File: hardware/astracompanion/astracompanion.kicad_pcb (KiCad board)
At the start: 2 copper layers, 118.5 x 94.8 mm, 124 parts, among them J1 Screw_Terminal_01x02, J10 Conn_01x03_Pin, J2 Screw_Terminal_01x02, J3 Conn_01x03_Pin, J4 USB_C_Receptacle_USB2.0, J5 Conn_01x02_Socket, J6 Micro_SD_Card, J7 Conn_01x04_Socket, J8 testpoint, J9 Encoder_L, Q1 2N3904, Q2 2N3904, Q3 2N7002, Q4 AO3401A, SW1 PTS645, SW2 SW_SPST, SW3 PTS645, SW4 Reset / EN button, SW5 Boot / IO0 button, SW6 PTS645, U1 MT3608_BOOSTER_MODULE, U10 MAX17048G+T10, U11 USBLC6-2SC6, U12 74AHCT125, U13 USBLC6-4SC6, U2 ESP32-S3-DEVKITC-1-N8R8, U3 DRV8833PWP, U4 MAX98357A, U5 MPU-6050, U6 DS3231M, U7 AP2112K-3.3, U8 VL53L0CXV0DH1

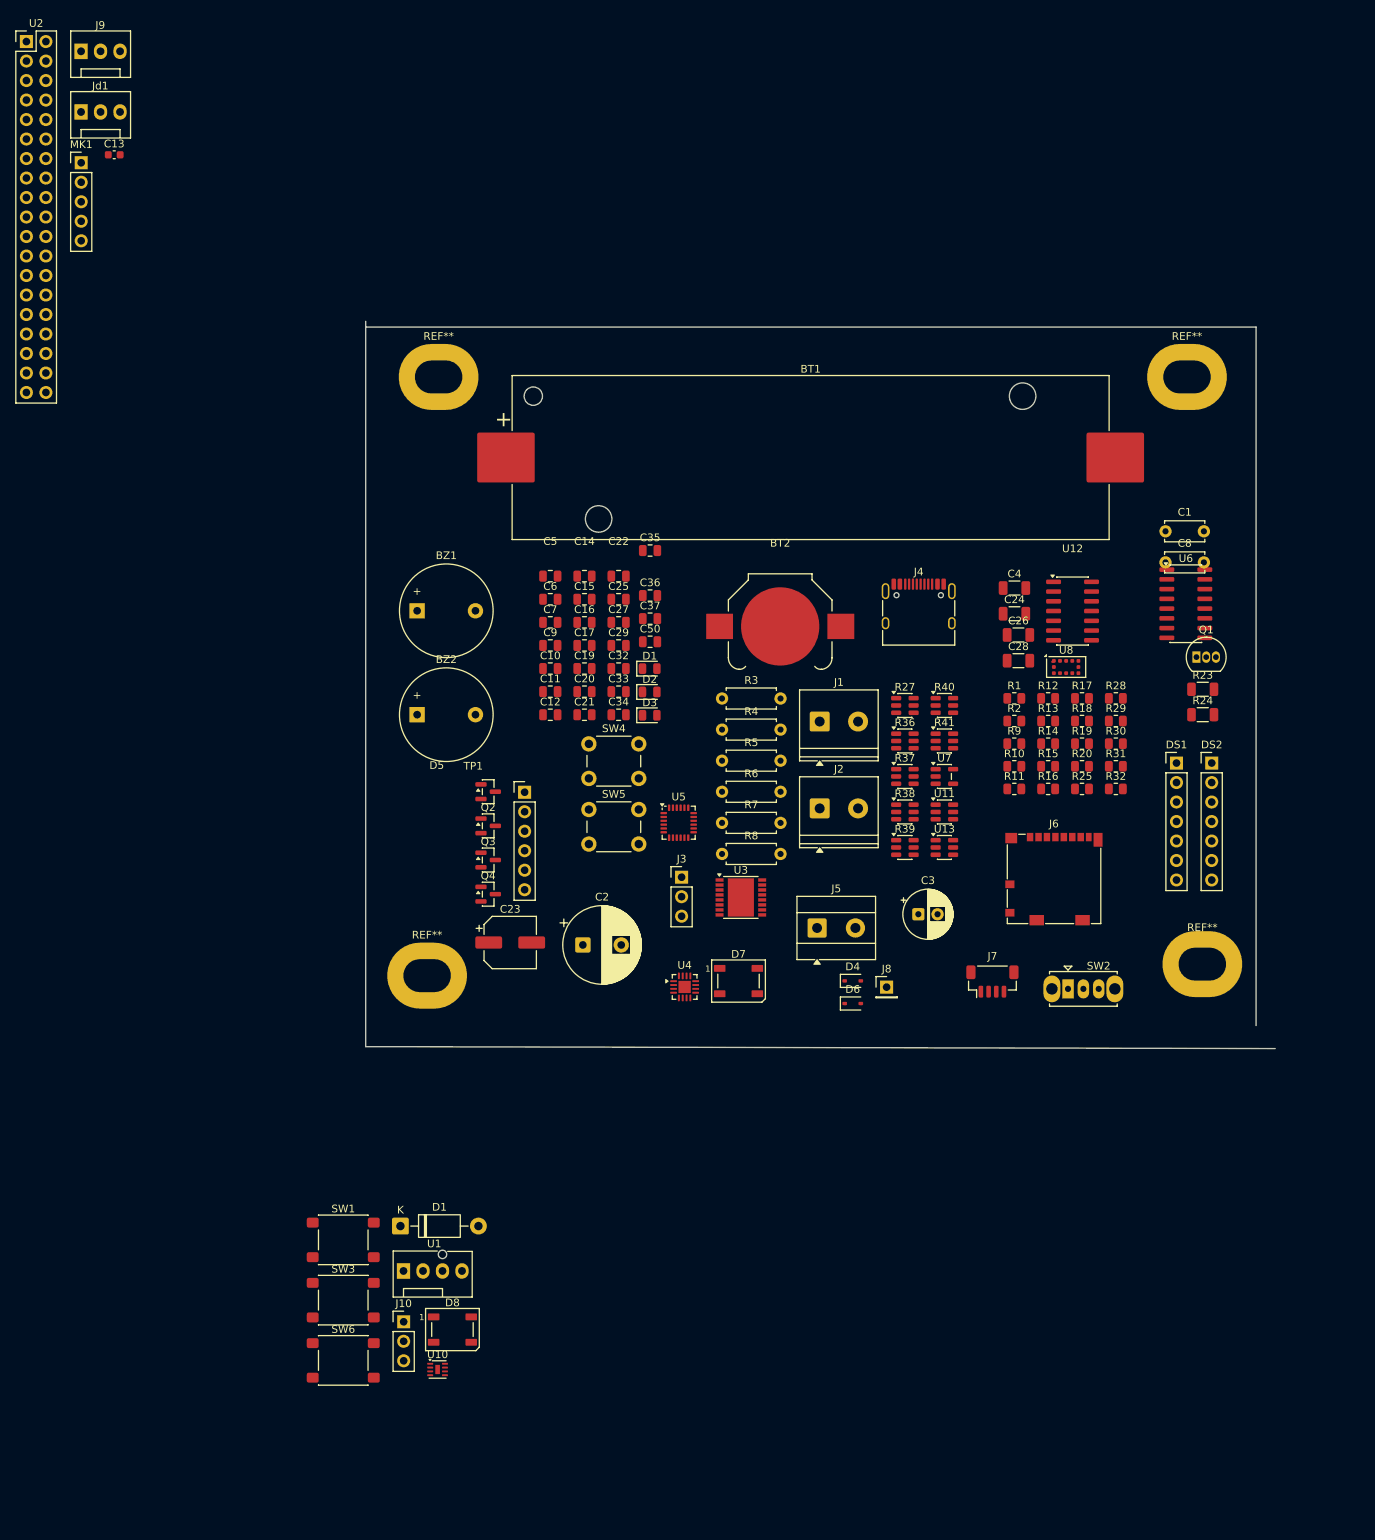
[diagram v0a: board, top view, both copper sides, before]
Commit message: Add firmware skeleton and document the current hardware
Co-authored-by: Cursor <cursoragent@cursor.com>
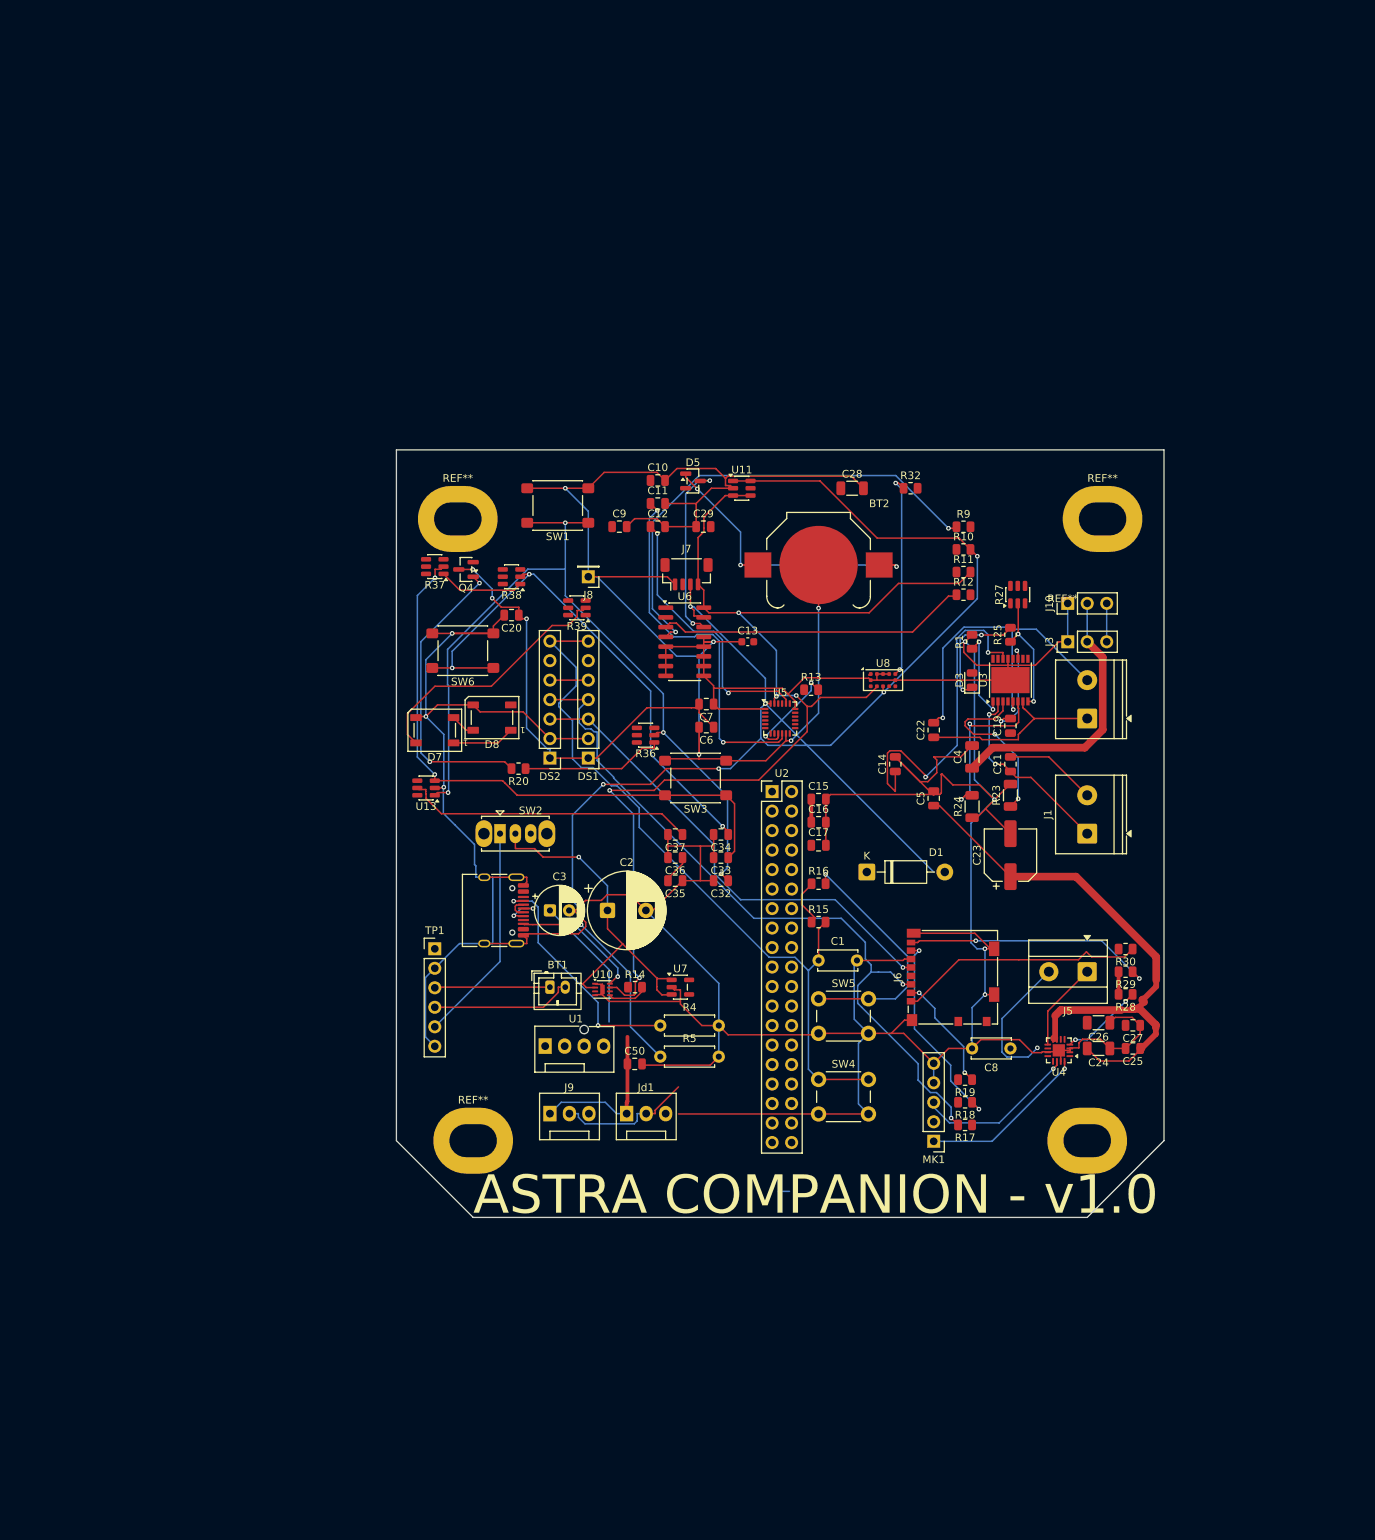
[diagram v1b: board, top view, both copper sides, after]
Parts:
- removed BZ1: Magnetic 5V Buzzer, Buzzer_Beeper:Buzzer_12x9.5RM7.6
- removed BZ2: Buzzer, Buzzer_Beeper:Buzzer_12x9.5RM7.6
- removed the D1 at (83.0, 83.5)
- removed the D1 at (50.5, 156.1)
- removed D2: RED, LED_SMD:LED_0805_2012Metric
- removed D4, D6: 1N4148WS, Diode_SMD:D_SOD-323
- removed Q1: 2N3904, Package_TO_SOT_THT:TO-92_Inline
- removed Q2: 2N3904, Package_TO_SOT_SMD:SOT-23
- removed Q3: 2N7002, Package_TO_SOT_SMD:SOT-23
- removed R2: 1k, Resistor_SMD:R_0805_2012Metric
- removed R3, R7: 10k, Resistor_THT:R_Axial_DIN0207_L6.3mm_D2.5mm_P7.62mm_Horizontal
- removed R31: 10k, Resistor_SMD:R_0805_2012Metric
- removed R40, R41: 330, Package_TO_SOT_SMD:SOT-23-6
- removed R6: 100, Resistor_THT:R_Axial_DIN0207_L6.3mm_D2.5mm_P7.62mm_Horizontal
- removed R8: 1k, Resistor_THT:R_Axial_DIN0207_L6.3mm_D2.5mm_P7.62mm_Horizontal
- removed the REF** at (155.0, 122.0)
- removed the REF** at (55.5, 45.5)
- removed the REF** at (153.0, 45.5)
- removed the REF** at (54.0, 123.5)
- removed U12: 74AHCT125, Package_SO:SOIC-14_3.9x8.7mm_P1.27mm
- added D1: 1N5819, Diode_THT:D_DO-41_SOD81_P10.16mm_Horizontal, F.Cu at (111.3, 110.0)
- added REF**: MountingHole_4.3x6.2mm_M4_Pad, MountingHole:MountingHole_4.3x6.2mm_M4_Pad, F.Cu at (60.0, 145.0)
- added REF**: MountingHole_4.3x6.2mm_M4_Pad, MountingHole:MountingHole_4.3x6.2mm_M4_Pad, F.Cu at (58.0, 64.0)
- added REF**: MountingHole_4.3x6.2mm_M4_Pad, MountingHole:MountingHole_4.3x6.2mm_M4_Pad, F.Cu at (142.0, 64.0)
- added REF**: MountingHole_4.3x6.2mm_M4_Pad, MountingHole:MountingHole_4.3x6.2mm_M4_Pad, F.Cu at (140.0, 145.0)
- BT1: footprint Battery:BatteryHolder_Keystone_1042_1x18650 -> Connector_JST:JST_PH_B2B-PH-K_1x02_P2.00mm_Vertical
- moved MK1 169.1 mm to (120.0, 145.1), turned to 180 degrees
- moved J9 151.3 mm to (70.0, 141.5)
- moved Jd1 148.6 mm to (80.0, 141.5)
- moved U2 137.8 mm to (99.0, 99.5)
- moved J10 127.5 mm to (137.5, 75.0), turned to 90 degrees
- moved C13 104.1 mm to (95.8, 80.0)
- moved SW1 99.7 mm to (71.0, 62.2), turned to 180 degrees
- moved SW6 93.8 mm to (58.7, 81.2), turned to 180 degrees
- moved C25 89.0 mm to (145.9, 133.0), turned to 180 degrees
- moved DS2 86.2 mm to (70.0, 95.2), turned to 180 degrees
- moved C27 85.1 mm to (145.9, 130.0), turned to 180 degrees
- moved SW3 82.1 mm to (89.0, 97.8), turned to 180 degrees
- moved D8 79.9 mm to (62.5, 89.9), turned to 180 degrees
- moved BT1 76.9 mm to (70.0, 125.0)
- moved SW2 76.7 mm to (63.5, 105.0)
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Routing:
- net GND: track 0.00 -> 793.9 mm, vias 0 -> 12
- net +5V: track 0.00 -> 174.2 mm
- net I2C_SDA: track 0.00 -> 160.5 mm, vias 0 -> 7
- net I2C_SCL: track 0.00 -> 150.1 mm, vias 0 -> 5
- net Net-(U13-I/O1): track 0.00 -> 105.7 mm, vias 0 -> 4
- net +3V3: track 0.00 -> 101.3 mm
- net SPI_MOSI: track 0.00 -> 96.4 mm, vias 0 -> 2
- net ESP_RST: track 0.00 -> 95.5 mm
- net Net-(U13-I/O2): track 0.00 -> 78.3 mm, vias 0 -> 2
- net BTN_DOWN: track 0.00 -> 70.6 mm, vias 0 -> 3
- net SPI_CLK: track 0.00 -> 62.6 mm, vias 0 -> 1
- net Net-(U6-~{RST}): track 0.00 -> 62.2 mm, vias 0 -> 2
- net +3V3_DISP: track 0.00 -> 58.6 mm, vias 0 -> 3
- net Net-(U5-REGOUT): track 0.00 -> 47.9 mm, vias 0 -> 2
- net VBAT: track 0.00 -> 45.5 mm, vias 0 -> 1
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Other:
- board size 118.5 x 94.8 mm -> 100 x 100 mm
- copper layers 2 -> 4
- board text added: "ASTRA COMPANION - v1.0"

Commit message: Ship the laptop voice stack, Phase 6 robot contract, and ESP32 firmware.
Local secrets, config, and databases stay gitignored.

Co-authored-by: Cursor <cursoragent@cursor.com>
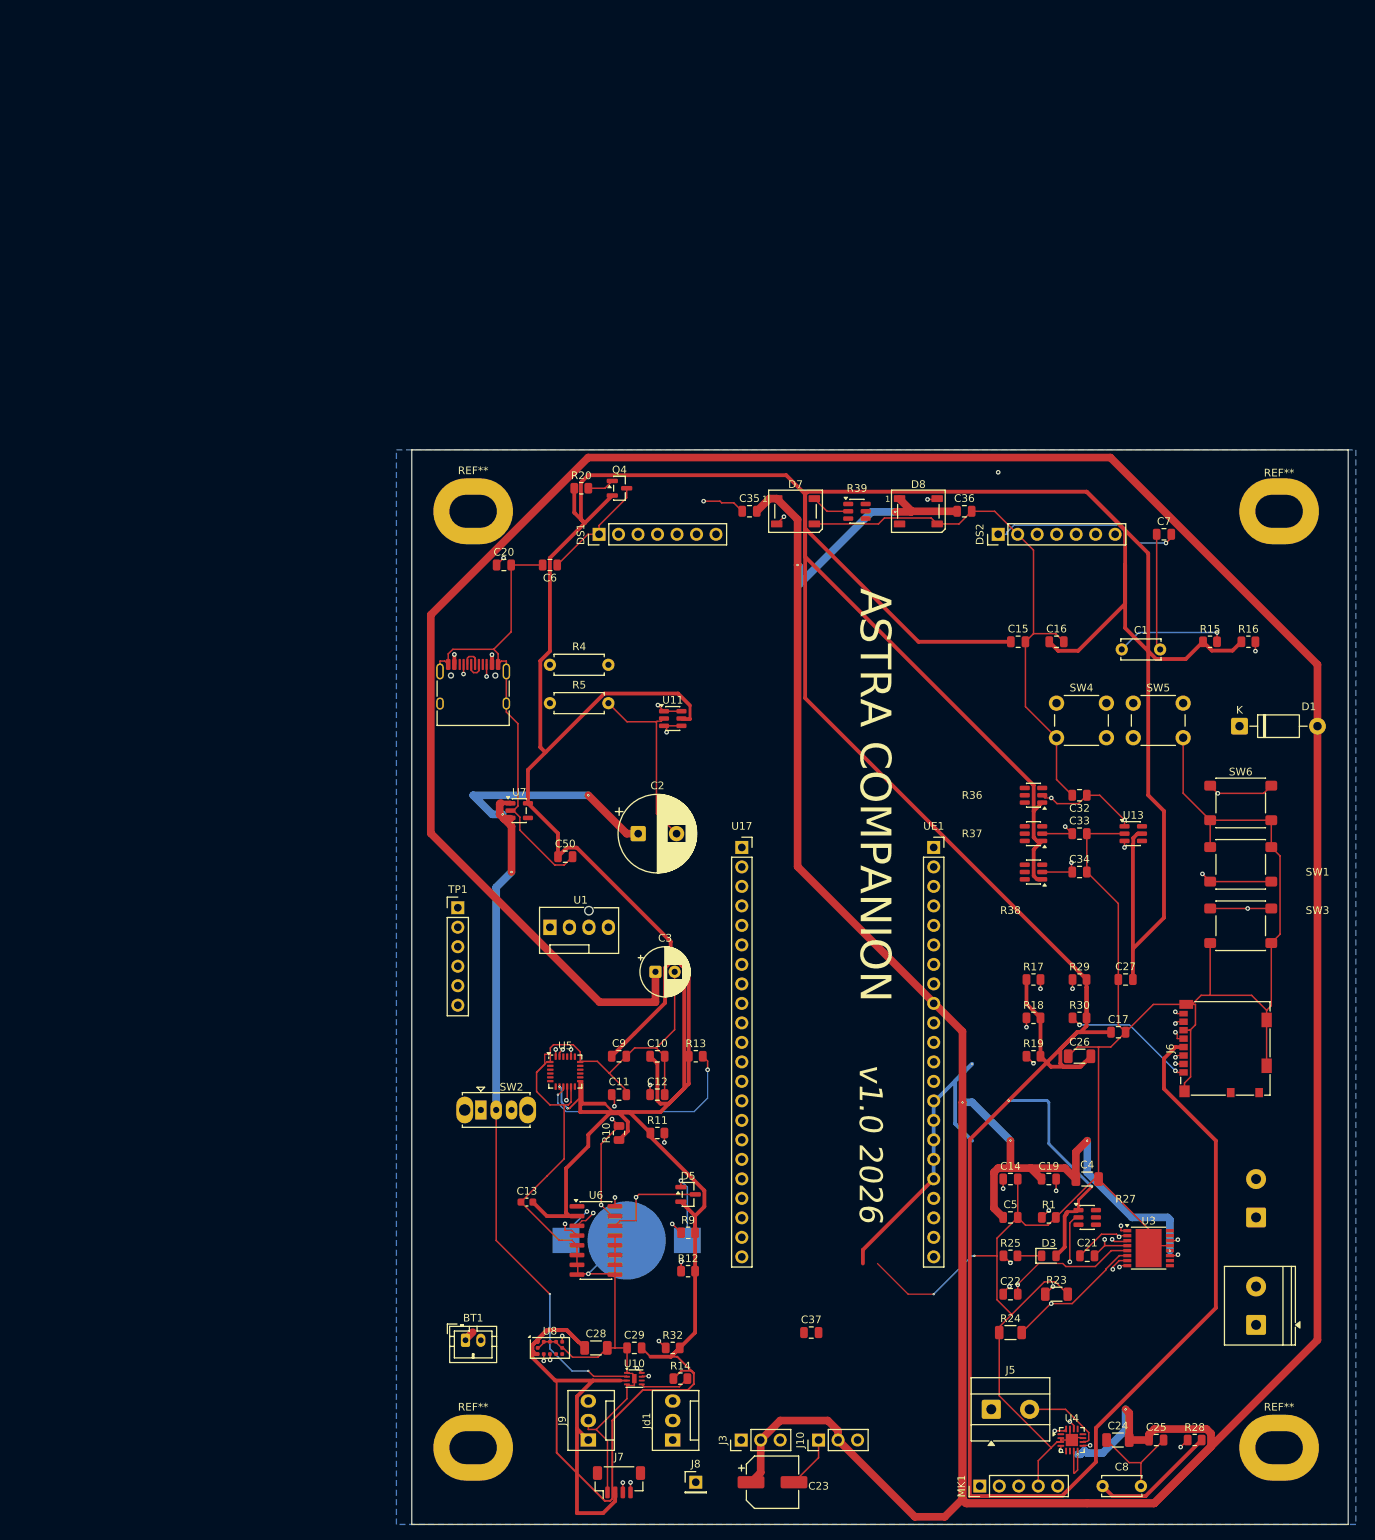
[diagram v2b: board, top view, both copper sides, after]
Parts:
- removed U2: ESP32-S3-DEVKITC-1-N8R8, Connector_PinHeader_2.54mm:PinHeader_2x19_P2.54mm_Vertical
- added U17: Conn_01x22_Pin, Connector_PinSocket_2.54mm:PinSocket_1x22_P2.54mm_Vertical, F.Cu at (95.0, 106.8)
- added UE1: Conn_01x22_Pin, Connector_PinSocket_2.54mm:PinSocket_1x22_P2.54mm_Vertical, F.Cu at (120.0, 106.8)
- BT2, J1: moved to B.Cu
- moved REF** 161.5 mm to (165.0, 185.0)
- moved REF** 146.2 mm to (60.0, 185.0)
- moved J8 118.8 mm to (89.0, 189.5), turned to 0 degrees
- moved J7 118.6 mm to (79.0, 189.5)
- moved C28 116.9 mm to (76.0, 172.0)
- moved R32 116.2 mm to (86.0, 172.0)
- moved J10 113.7 mm to (105.0, 184.0)
- moved J3 112.4 mm to (94.9, 184.0)
- moved C29 107.4 mm to (81.0, 172.0)
- moved SW6 103.3 mm to (160.0, 101.0), turned to 0 degrees
- moved SW1 100.5 mm to (160.0, 109.0)
- moved R9 98.7 mm to (88.0, 157.0)
- moved U8 97.2 mm to (70.0, 172.0)
- moved R12 95.2 mm to (88.0, 162.0)
- moved D5 93.0 mm to (88.0, 152.0)
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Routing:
- net +3V3: track 101.3 -> 1040.0 mm, vias 0 -> 4
- net +5V: track 174.2 -> 742.7 mm, vias 0 -> 8
- net SPI_CLK: track 62.6 -> 137.4 mm
- net VBAT: track 45.5 -> 117.8 mm, vias 1 -> 5
- net Net-(U13-I/O1): track 105.7 -> 36.2 mm, vias 4 -> 3
- net +3V3_DISP: track 58.6 -> 118.1 mm
- net GND: track 793.9 -> 847.8 mm, vias 12 -> 4
- net TFT_DC: track 5.00 -> 58.4 mm
- net SPI_MOSI: track 96.4 -> 147.9 mm
- net VBUS: track 0.00 -> 47.1 mm, vias 0 -> 2
- net Net-(U6-~{RST}): track 62.2 -> 18.3 mm
- net unconnected-(UE1-Pin_22-Pad22): track 0.00 -> 43.7 mm, vias 0 -> 2
- net B+: track 15.0 -> 55.8 mm
- net Net-(U5-REGOUT): track 47.9 -> 10.1 mm
- net Net-(U13-I/O2): track 78.3 -> 42.2 mm, vias 2 -> 3
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- added copper zone on In2.Cu, net +3V3
- added copper zone on B.Cu, net GND
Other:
- board size 100 x 100 mm -> 122 x 140 mm
- board text added: "ASTRA"
- board text added: "ASTRA COMPANION"
- board text added: "v1.0 2026"
- board text removed: "ASTRA COMPANION - v1.0"
